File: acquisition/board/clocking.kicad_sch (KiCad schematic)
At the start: 59 parts, among them U11 LMK04806, U12 AK5DAF1-100.0000T2, U14 74AVCH1T45, U15 74AVCH1T45, U16 74AVCH1T45, U17 74AVCH1T45, U19 74AVCH1T45, U20 74AVCH1T45

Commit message: Finished footprint assignment
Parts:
- L1: footprint (none) -> azonenberg_pcb:EIA_0603_INDUCTOR_NOSILK
- U11: footprint (none) -> azonenberg_pcb:QFN_64_0.5MM_9x9MM
- U12: footprint (none) -> azonenberg_pcb:OSCILLATOR_LVDS_5.0x3.2
- U14, U15, U16, U17, U19, U20: footprint (none) -> azonenberg_pcb:DFN_6_0.5MM_1.45x1.00MM
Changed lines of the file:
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@@
   (title_block
     (title "Digitizer board")
-    (date "2022-07-17")
+    (date "2023-01-29")
     (rev "0.1")
     (company "A. Zonenberg")
@@
       (effects (font (size 1.27 1.27)) (justify left))
     )
-    (property "Footprint" "" (id 2) (at 165.1 161.29 0)
+    (property "Footprint" "azonenberg_pcb:QFN_64_0.5MM_9x9MM" (id 2) (at 165.1 161.29 0)
       (effects (font (size 1.27 1.27)) hide)
     )
@@
       (effects (font (size 1.524 1.524)))
     )
-    (property "Footprint" "" (id 2) (at 237.49 74.93 0)
+    (property "Footprint" "azonenberg_pcb:DFN_6_0.5MM_1.45x1.00MM" (id 2) (at 237.49 74.93 0)
       (effects (font (size 1.524 1.524)) hide)
     )
@@
       (effects (font (size 1.016 1.016)))
     )
-    (property "Footprint" "" (id 2) (at 33.02 63.5 0)
+    (property "Footprint" "azonenberg_pcb:EIA_0603_INDUCTOR_NOSILK" (id 2) (at 33.02 63.5 0)
       (effects (font (size 1.524 1.524)) hide)
     )
@@
       (effects (font (size 1.524 1.524)))
     )
-    (property "Footprint" "" (id 2) (at 237.49 128.27 0)
+    (property "Footprint" "azonenberg_pcb:DFN_6_0.5MM_1.45x1.00MM" (id 2) (at 237.49 128.27 0)
       (effects (font (size 1.524 1.524)) hide)
     )
@@
       (effects (font (size 1.524 1.524)))
     )
-    (property "Footprint" "" (id 2) (at 237.49 39.37 0)
+    (property "Footprint" "azonenberg_pcb:DFN_6_0.5MM_1.45x1.00MM" (id 2) (at 237.49 39.37 0)
       (effects (font (size 1.524 1.524)) hide)
     )
@@
     (property "Reference" "U11" (id 0) (at 130.81 20.2905 0))
     (property "Value" "LMK04806" (id 1) (at 130.81 23.0656 0))
-    (property "Footprint" "" (id 2) (at 115.57 128.27 0)
+    (property "Footprint" "azonenberg_pcb:QFN_64_0.5MM_9x9MM" (id 2) (at 115.57 128.27 0)
       (effects (font (size 1.27 1.27)) hide)
     )
@@
       (effects (font (size 1.524 1.524)))
     )
-    (property "Footprint" "" (id 2) (at 43.18 46.99 0)
+    (property "Footprint" "azonenberg_pcb:OSCILLATOR_LVDS_5.0x3.2" (id 2) (at 43.18 46.99 0)
       (effects (font (size 1.524 1.524)) hide)
     )
@@
       (effects (font (size 1.524 1.524)))
     )
-    (property "Footprint" "" (id 2) (at 237.49 57.15 0)
+    (property "Footprint" "azonenberg_pcb:DFN_6_0.5MM_1.45x1.00MM" (id 2) (at 237.49 57.15 0)
       (effects (font (size 1.524 1.524)) hide)
     )
@@
     (property "Reference" "U11" (id 0) (at 90.805 135.8605 0))
     (property "Value" "LMK04806" (id 1) (at 90.805 138.6356 0))
-    (property "Footprint" "" (id 2) (at 76.2 180.34 0)
+    (property "Footprint" "azonenberg_pcb:QFN_64_0.5MM_9x9MM" (id 2) (at 76.2 180.34 0)
       (effects (font (size 1.27 1.27)) hide)
     )
@@
       (effects (font (size 1.524 1.524)))
     )
-    (property "Footprint" "" (id 2) (at 237.49 110.49 0)
+    (property "Footprint" "azonenberg_pcb:DFN_6_0.5MM_1.45x1.00MM" (id 2) (at 237.49 110.49 0)
       (effects (font (size 1.524 1.524)) hide)
     )
@@
       (effects (font (size 1.524 1.524)))
     )
-    (property "Footprint" "" (id 2) (at 237.49 92.71 0)
+    (property "Footprint" "azonenberg_pcb:DFN_6_0.5MM_1.45x1.00MM" (id 2) (at 237.49 92.71 0)
       (effects (font (size 1.524 1.524)) hide)
     )

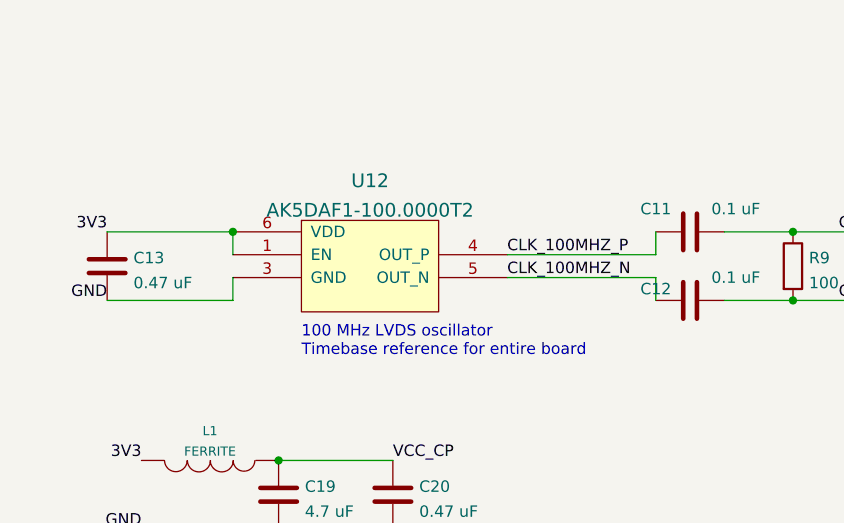
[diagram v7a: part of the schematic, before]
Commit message: Began layout of clocking subsystem
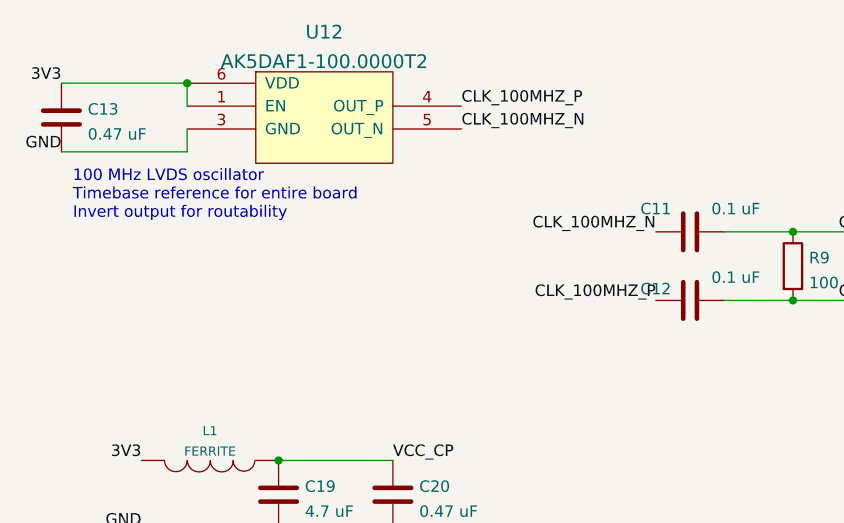
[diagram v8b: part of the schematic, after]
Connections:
- net CLK_100MHZ_N: now also C11.1; no longer C12.1
- net CLK_100MHZ_P: now also C12.1; no longer C11.1
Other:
- note added: "100 MHz LVDS oscillator Timebase reference for entire board Invert output for routability"
- note removed: "100 MHz LVDS oscillator Timebase reference for entire board"
- moved on the sheet: C13, U12
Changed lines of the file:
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@@
   (title_block
     (title "Digitizer board")
-    (date "2023-01-31")
+    (date "2023-02-01")
     (rev "0.1")
     (company "A. Zonenberg")
@@
   (junction (at 242.57 154.94) (diameter 0) (color 0 0 0 0)
   )
-  (junction (at 35.56 38.1) (diameter 0) (color 0 0 0 0)
+  (junction (at 30.48 21.59) (diameter 0) (color 0 0 0 0)
   )
   (junction (at 215.9 135.89) (diameter 0) (color 0 0 0 0)
@@
     (stroke (width 0) (type default) (color 0 0 0 0))
   )
-  (wire (pts (xy 21.59 45.72) (xy 35.56 45.72))
+  (wire (pts (xy 16.51 29.21) (xy 30.48 29.21))
     (stroke (width 0) (type default) (color 0 0 0 0))
   )
@@
     (stroke (width 0) (type default) (color 0 0 0 0))
   )
-  (wire (pts (xy 66.04 43.18) (xy 82.55 43.18))
-    (stroke (width 0) (type default) (color 0 0 0 0))
-  )
   (wire (pts (xy 125.73 133.35) (xy 125.73 135.89))
     (stroke (width 0) (type default) (color 0 0 0 0))
@@
     (stroke (width 0) (type default) (color 0 0 0 0))
   )
-  (wire (pts (xy 82.55 40.64) (xy 82.55 38.1))
-    (stroke (width 0) (type default) (color 0 0 0 0))
-  )
-  (wire (pts (xy 82.55 43.18) (xy 82.55 45.72))
-    (stroke (width 0) (type default) (color 0 0 0 0))
-  )
   (wire (pts (xy 256.54 135.89) (xy 270.51 135.89))
     (stroke (width 0) (type default) (color 0 0 0 0))
@@
     (stroke (width 0) (type default) (color 0 0 0 0))
   )
-  (wire (pts (xy 35.56 38.1) (xy 35.56 40.64))
+  (wire (pts (xy 30.48 21.59) (xy 30.48 24.13))
     (stroke (width 0) (type default) (color 0 0 0 0))
   )
@@
     (stroke (width 0) (type default) (color 0 0 0 0))
   )
-  (wire (pts (xy 35.56 45.72) (xy 35.56 43.18))
+  (wire (pts (xy 30.48 29.21) (xy 30.48 26.67))
     (stroke (width 0) (type default) (color 0 0 0 0))
   )
@@
     (stroke (width 0) (type default) (color 0 0 0 0))
   )
-  (wire (pts (xy 66.04 40.64) (xy 82.55 40.64))
-    (stroke (width 0) (type default) (color 0 0 0 0))
-  )
   (wire (pts (xy 25.4 82.55) (xy 39.37 82.55))
     (stroke (width 0) (type default) (color 0 0 0 0))
   )
-  (wire (pts (xy 21.59 38.1) (xy 35.56 38.1))
+  (wire (pts (xy 16.51 21.59) (xy 30.48 21.59))
     (stroke (width 0) (type default) (color 0 0 0 0))
   )
@@
     (stroke (width 0) (type default) (color 0 0 0 0))
   )
-  (text "100 MHz LVDS oscillator\nTimebase reference for entire board"
-    (at 43.18 52.07 0)
+  (text "100 MHz LVDS oscillator\nTimebase reference for entire board\nInvert output for routability"
+    (at 17.78 36.83 0)
     (effects (font (size 1.27 1.27)) (justify left bottom))
   )
@@
     (effects (font (size 1.27 1.27)) (justify right bottom))
   )
+  (label "CLK_100MHZ_P" (at 82.55 45.72 180)
+    (effects (font (size 1.27 1.27)) (justify right bottom))
+  )
   (label "1V8" (at 232.41 119.38 180)
     (effects (font (size 1.27 1.27)) (justify right bottom))
@@
     (effects (font (size 1.27 1.27)) (justify left bottom))
   )
-  (label "3V3" (at 21.59 38.1 180)
+  (label "3V3" (at 16.51 21.59 180)
     (effects (font (size 1.27 1.27)) (justify right bottom))
   )
@@
     (effects (font (size 1.27 1.27)) (justify right bottom))
   )
-  (label "CLK_100MHZ_N" (at 66.04 43.18 0)
+  (label "CLK_100MHZ_N" (at 60.96 26.67 0)
     (effects (font (size 1.27 1.27)) (justify left bottom))
   )
@@
     (effects (font (size 1.27 1.27)) (justify right bottom))
   )
-  (label "CLK_100MHZ_P" (at 66.04 40.64 0)
+  (label "CLK_100MHZ_P" (at 60.96 24.13 0)
     (effects (font (size 1.27 1.27)) (justify left bottom))
   )
@@
     (effects (font (size 1.27 1.27)) (justify left bottom))
   )
+  (label "CLK_100MHZ_N" (at 82.55 38.1 180)
+    (effects (font (size 1.27 1.27)) (justify right bottom))
+  )
   (label "STATUS_CLKIN0" (at 162.56 157.48 180)
     (effects (font (size 1.27 1.27)) (justify right bottom))
@@
     (effects (font (size 1.27 1.27)) (justify right bottom))
   )
-  (label "GND" (at 21.59 45.72 180)
+  (label "GND" (at 16.51 29.21 180)
     (effects (font (size 1.27 1.27)) (justify right bottom))
   )
@@
     (pin "2")
   )
-  (symbol (lib_id "osc-azonenberg:OSC_LVDS_NOPAD") (at 43.18 46.99 0) (unit 1)
-    (in_bom yes) (on_board yes) (fields_autoplaced)
-    (property "Reference" "U12" (id 0) (at 50.8 32.4261 0)
+  (symbol (lib_id "osc-azonenberg:OSC_LVDS_NOPAD") (at 38.1 30.48 0) (unit 1)
+    (in_bom yes) (on_board yes) (fields_autoplaced)
+    (property "Reference" "U12" (id 0) (at 45.72 15.9161 0)
       (effects (font (size 1.524 1.524)))
     )
-    (property "Value" "AK5DAF1-100.0000T2" (id 1) (at 50.8 35.7051 0)
+    (property "Value" "AK5DAF1-100.0000T2" (id 1) (at 45.72 19.1951 0)
       (effects (font (size 1.524 1.524)))
     )
-    (property "Footprint" "azonenberg_pcb:OSCILLATOR_LVDS_5.0x3.2" (id 2) (at 43.18 46.99 0)
+    (property "Footprint" "azonenberg_pcb:OSCILLATOR_LVDS_5.0x3.2" (id 2) (at 38.1 30.48 0)
       (effects (font (size 1.524 1.524)) hide)
     )
-    (property "Datasheet" "" (id 3) (at 43.18 46.99 0)
+    (property "Datasheet" "" (id 3) (at 38.1 30.48 0)
       (effects (font (size 1.524 1.524)))
     )
@@
     (pin "PAD")
   )
-  (symbol (lib_id "device:C") (at 21.59 41.91 0) (unit 1)
-    (in_bom yes) (on_board yes) (fields_autoplaced)
-    (property "Reference" "C13" (id 0) (at 24.511 41.0015 0)
-      (effects (font (size 1.27 1.27)) (justify left))
-    )
-    (property "Value" "0.47 uF" (id 1) (at 24.511 43.7766 0)
-      (effects (font (size 1.27 1.27)) (justify left))
-    )
-    (property "Footprint" "azonenberg_pcb:EIA_0402_CAP_NOSILK" (id 2) (at 22.5552 45.72 0)
-      (effects (font (size 1.27 1.27)) hide)
-    )
-    (property "Datasheet" "" (id 3) (at 21.59 41.91 0)
-      (effects (font (size 1.27 1.27)) hide)
-    )
+  (symbol (lib_id "device:C") (at 16.51 25.4 0) (unit 1)
+    (in_bom yes) (on_board yes) (fields_autoplaced)
+    (property "Reference" "C13" (id 0) (at 19.431 24.4915 0)
+      (effects (font (size 1.27 1.27)) (justify left))
+    )
+    (property "Value" "0.47 uF" (id 1) (at 19.431 27.2666 0)
+      (effects (font (size 1.27 1.27)) (justify left))
+    )
+    (property "Footprint" "azonenberg_pcb:EIA_0402_CAP_NOSILK" (id 2) (at 17.4752 29.21 0)
+      (effects (font (size 1.27 1.27)) hide)
+    )
+    (property "Datasheet" "" (id 3) (at 16.51 25.4 0)
+      (effects (font (size 1.27 1.27)) hide)
+    )
